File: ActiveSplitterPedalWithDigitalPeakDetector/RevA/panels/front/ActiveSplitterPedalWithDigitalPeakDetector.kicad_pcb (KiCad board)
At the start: 2 copper layers, 112.5 x 86.4 mm, 5 parts

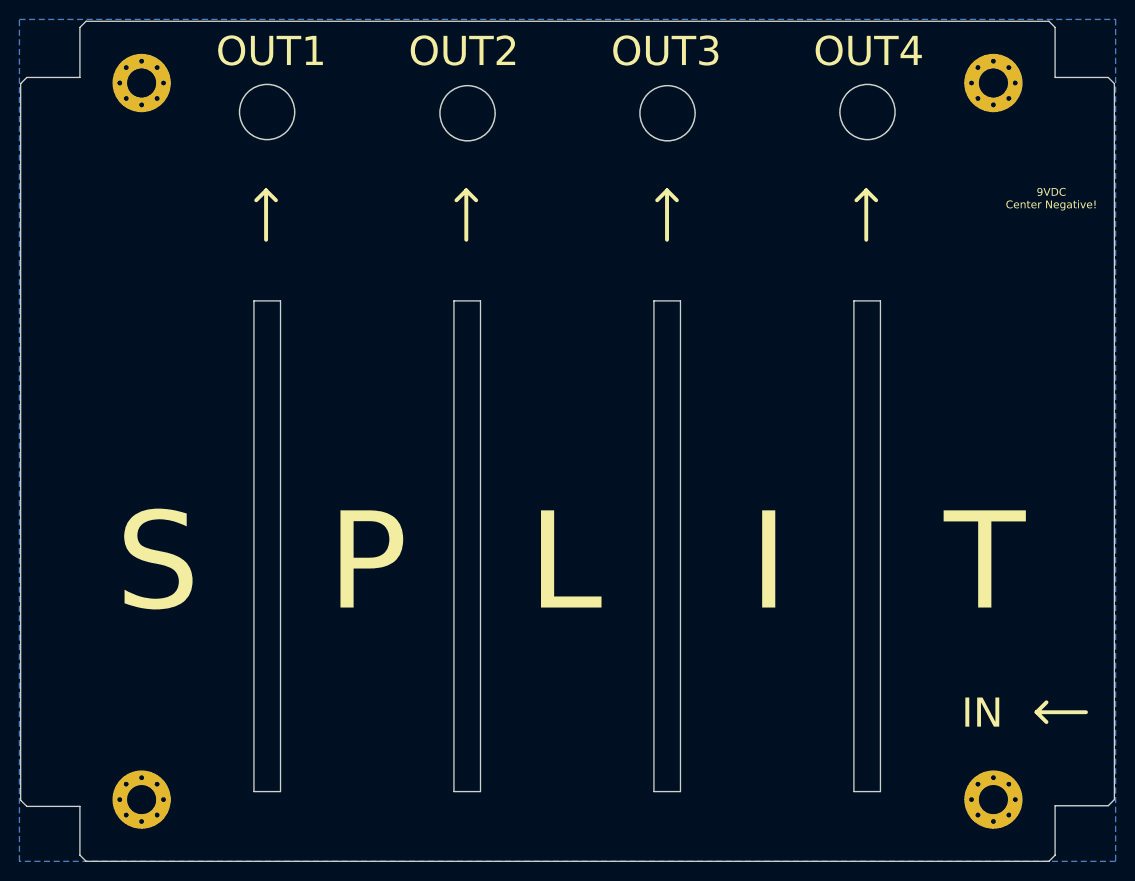
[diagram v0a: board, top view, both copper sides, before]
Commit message: updated front/back panel layout and gerbers
- Changed mount holes to non-via
- Changed BCu plane to FCu plane (same side as FCu silkscreen)
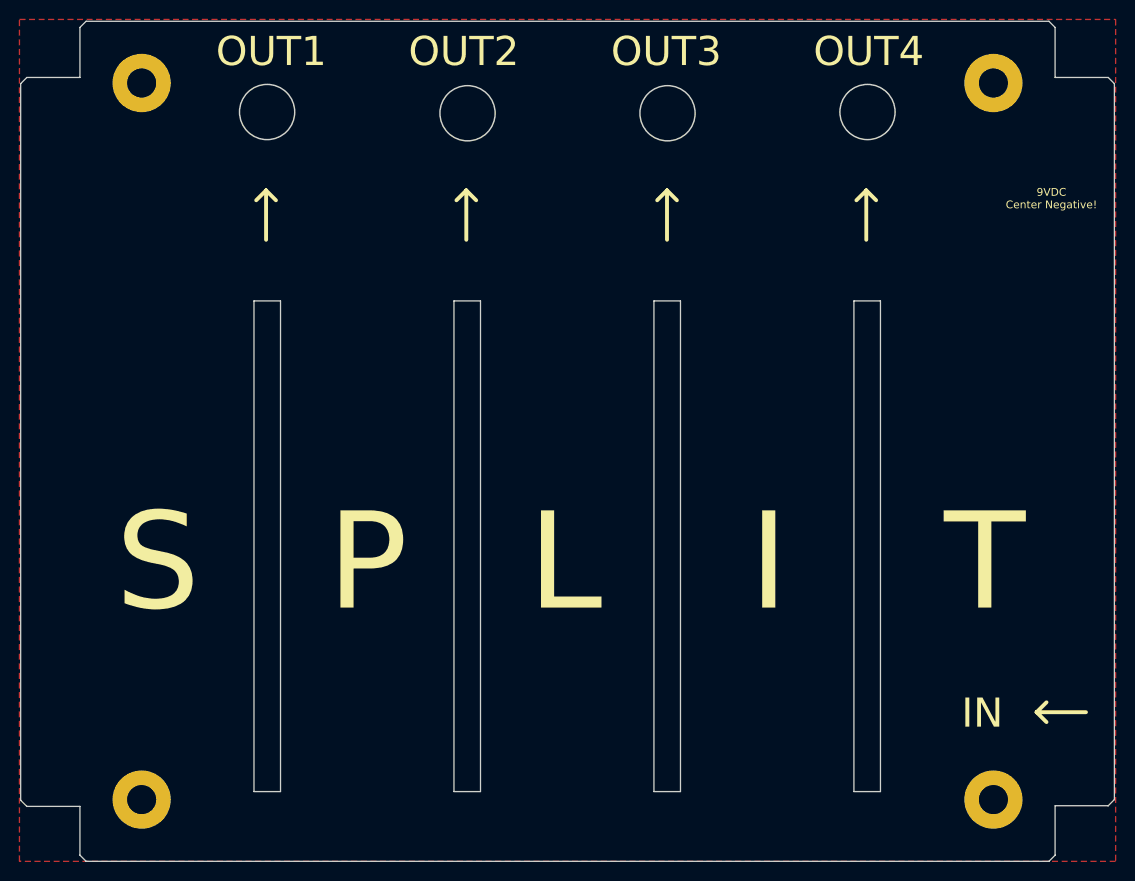
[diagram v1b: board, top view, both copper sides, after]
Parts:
- removed the REF** at (92.3, 124.7)
- removed the REF** at (180.0, 124.7)
- removed the REF** at (180.0, 51.0)
- added REF**: MountingHole_3mm_Pad, MountingHole:MountingHole_3mm_Pad, F.Cu at (180.0, 51.0)
- added REF**: MountingHole_3mm_Pad, MountingHole:MountingHole_3mm_Pad, F.Cu at (180.0, 124.7)
- added REF**: MountingHole_3mm_Pad, MountingHole:MountingHole_3mm_Pad, F.Cu at (92.3, 124.7)
- REF**: value MountingHole_3mm_Pad_Via -> MountingHole_3mm_Pad; footprint MountingHole:MountingHole_3mm_Pad_Via -> MountingHole:MountingHole_3mm_Pad
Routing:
- added copper zone on F.Cu, net (none)
- removed copper zone on B.Cu, net (none)
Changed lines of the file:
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@@
     (diff_pair_gap 0.127)
   )
-  (module MountingHole:MountingHole_3mm_Pad_Via locked (layer F.Cu)
+  (module MountingHole:MountingHole_3mm_Pad locked (layer F.Cu)
+    (at 179.959 50.9905)
+    (descr "Mounting Hole 3mm")
+    (tags "mounting hole 3mm")
+    (attr virtual)
+    (fp_text reference REF** (at 0 -4) (layer F.SilkS) hide
+      (effects (font (size 1 1) (thickness 0.15)))
+    )
+    (fp_text value MountingHole_3mm_Pad (at 0 4) (layer F.Fab)
+      (effects (font (size 1 1) (thickness 0.15)))
+    )
+    (fp_circle (center 0 0) (end 3.25 0) (layer F.CrtYd) (width 0.05))
+    (fp_circle (center 0 0) (end 3 0) (layer Cmts.User) (width 0.15))
+    (fp_text user %R (at 0.3 0) (layer F.Fab)
+      (effects (font (size 1 1) (thickness 0.15)))
+    )
+    (pad 1 thru_hole circle (at 0 0) (size 6 6) (drill 3) (layers *.Cu *.Mask))
+  )
+  (module MountingHole:MountingHole_3mm_Pad locked (layer F.Cu)
+    (at 179.959 124.714)
+    (descr "Mounting Hole 3mm")
+    (tags "mounting hole 3mm")
+    (attr virtual)
+    (fp_text reference REF** (at 0 -4) (layer F.SilkS) hide
+      (effects (font (size 1 1) (thickness 0.15)))
+    )
+    (fp_text value MountingHole_3mm_Pad (at 0 4) (layer F.Fab)
+      (effects (font (size 1 1) (thickness 0.15)))
+    )
+    (fp_circle (center 0 0) (end 3.25 0) (layer F.CrtYd) (width 0.05))
+    (fp_circle (center 0 0) (end 3 0) (layer Cmts.User) (width 0.15))
+    (fp_text user %R (at 0.3 0) (layer F.Fab)
+      (effects (font (size 1 1) (thickness 0.15)))
+    )
+    (pad 1 thru_hole circle (at 0 0) (size 6 6) (drill 3) (layers *.Cu *.Mask))
+  )
+  (module MountingHole:MountingHole_3mm_Pad locked (layer F.Cu)
     (at 92.329 124.714)
     (descr "Mounting Hole 3mm")
@@
       (effects (font (size 1 1) (thickness 0.15)))
     )
-    (fp_text value MountingHole_3mm_Pad_Via (at 0 4) (layer F.Fab)
-      (effects (font (size 1 1) (thickness 0.15)))
-    )
-    (fp_circle (center 0 0) (end 3.25 0) (layer F.CrtYd) (width 0.05))
-    (fp_circle (center 0 0) (end 3 0) (layer Cmts.User) (width 0.15))
-    (fp_text user %R (at 0.3 0) (layer F.Fab)
-      (effects (font (size 1 1) (thickness 0.15)))
-    )
-    (pad 1 thru_hole circle (at 0 0) (size 6 6) (drill 3) (layers *.Cu *.Mask))
-    (pad 1 thru_hole circle (at 2.25 0) (size 0.8 0.8) (drill 0.5) (layers *.Cu *.Mask))
-    (pad 1 thru_hole circle (at 1.59099 1.59099) (size 0.8 0.8) (drill 0.5) (layers *.Cu *.Mask))
-    (pad 1 thru_hole circle (at 0 2.25) (size 0.8 0.8) (drill 0.5) (layers *.Cu *.Mask))
-    (pad 1 thru_hole circle (at -1.59099 1.59099) (size 0.8 0.8) (drill 0.5) (layers *.Cu *.Mask))
-    (pad 1 thru_hole circle (at -2.25 0) (size 0.8 0.8) (drill 0.5) (layers *.Cu *.Mask))
-    (pad 1 thru_hole circle (at -1.59099 -1.59099) (size 0.8 0.8) (drill 0.5) (layers *.Cu *.Mask))
-    (pad 1 thru_hole circle (at 0 -2.25) (size 0.8 0.8) (drill 0.5) (layers *.Cu *.Mask))
-    (pad 1 thru_hole circle (at 1.59099 -1.59099) (size 0.8 0.8) (drill 0.5) (layers *.Cu *.Mask))
-  )
-  (module MountingHole:MountingHole_3mm_Pad_Via locked (layer F.Cu)
-    (at 179.959 124.714)
-    (descr "Mounting Hole 3mm")
-    (tags "mounting hole 3mm")
-    (attr virtual)
-    (fp_text reference REF** (at 0 -4) (layer F.SilkS) hide
-      (effects (font (size 1 1) (thickness 0.15)))
-    )
-    (fp_text value MountingHole_3mm_Pad_Via (at 0 4) (layer F.Fab)
-      (effects (font (size 1 1) (thickness 0.15)))
-    )
-    (fp_circle (center 0 0) (end 3.25 0) (layer F.CrtYd) (width 0.05))
-    (fp_circle (center 0 0) (end 3 0) (layer Cmts.User) (width 0.15))
-    (fp_text user %R (at 0.3 0) (layer F.Fab)
-      (effects (font (size 1 1) (thickness 0.15)))
-    )
-    (pad 1 thru_hole circle (at 0 0) (size 6 6) (drill 3) (layers *.Cu *.Mask))
-    (pad 1 thru_hole circle (at 2.25 0) (size 0.8 0.8) (drill 0.5) (layers *.Cu *.Mask))
-    (pad 1 thru_hole circle (at 1.59099 1.59099) (size 0.8 0.8) (drill 0.5) (layers *.Cu *.Mask))
-    (pad 1 thru_hole circle (at 0 2.25) (size 0.8 0.8) (drill 0.5) (layers *.Cu *.Mask))
-    (pad 1 thru_hole circle (at -1.59099 1.59099) (size 0.8 0.8) (drill 0.5) (layers *.Cu *.Mask))
-    (pad 1 thru_hole circle (at -2.25 0) (size 0.8 0.8) (drill 0.5) (layers *.Cu *.Mask))
-    (pad 1 thru_hole circle (at -1.59099 -1.59099) (size 0.8 0.8) (drill 0.5) (layers *.Cu *.Mask))
-    (pad 1 thru_hole circle (at 0 -2.25) (size 0.8 0.8) (drill 0.5) (layers *.Cu *.Mask))
-    (pad 1 thru_hole circle (at 1.59099 -1.59099) (size 0.8 0.8) (drill 0.5) (layers *.Cu *.Mask))
-  )
-  (module MountingHole:MountingHole_3mm_Pad_Via locked (layer F.Cu)
-    (at 179.959 50.9905)
-    (descr "Mounting Hole 3mm")
-    (tags "mounting hole 3mm")
-    (attr virtual)
-    (fp_text reference REF** (at 0 -4) (layer F.SilkS) hide
-      (effects (font (size 1 1) (thickness 0.15)))
-    )
-    (fp_text value MountingHole_3mm_Pad_Via (at 0 4) (layer F.Fab)
-      (effects (font (size 1 1) (thickness 0.15)))
-    )
-    (fp_circle (center 0 0) (end 3.25 0) (layer F.CrtYd) (width 0.05))
-    (fp_circle (center 0 0) (end 3 0) (layer Cmts.User) (width 0.15))
-    (fp_text user %R (at 0.3 0) (layer F.Fab)
-      (effects (font (size 1 1) (thickness 0.15)))
-    )
-    (pad 1 thru_hole circle (at 0 0) (size 6 6) (drill 3) (layers *.Cu *.Mask))
-    (pad 1 thru_hole circle (at 2.25 0) (size 0.8 0.8) (drill 0.5) (layers *.Cu *.Mask))
-    (pad 1 thru_hole circle (at 1.59099 1.59099) (size 0.8 0.8) (drill 0.5) (layers *.Cu *.Mask))
-    (pad 1 thru_hole circle (at 0 2.25) (size 0.8 0.8) (drill 0.5) (layers *.Cu *.Mask))
-    (pad 1 thru_hole circle (at -1.59099 1.59099) (size 0.8 0.8) (drill 0.5) (layers *.Cu *.Mask))
-    (pad 1 thru_hole circle (at -2.25 0) (size 0.8 0.8) (drill 0.5) (layers *.Cu *.Mask))
-    (pad 1 thru_hole circle (at -1.59099 -1.59099) (size 0.8 0.8) (drill 0.5) (layers *.Cu *.Mask))
-    (pad 1 thru_hole circle (at 0 -2.25) (size 0.8 0.8) (drill 0.5) (layers *.Cu *.Mask))
-    (pad 1 thru_hole circle (at 1.59099 -1.59099) (size 0.8 0.8) (drill 0.5) (layers *.Cu *.Mask))
-  )
-  (module MountingHole:MountingHole_3mm_Pad_Via locked (layer F.Cu)
+    (fp_text value MountingHole_3mm_Pad (at 0 4) (layer F.Fab)
+      (effects (font (size 1 1) (thickness 0.15)))
+    )
+    (fp_circle (center 0 0) (end 3.25 0) (layer F.CrtYd) (width 0.05))
+    (fp_circle (center 0 0) (end 3 0) (layer Cmts.User) (width 0.15))
+    (fp_text user %R (at 0.3 0) (layer F.Fab)
+      (effects (font (size 1 1) (thickness 0.15)))
+    )
+    (pad 1 thru_hole circle (at 0 0) (size 6 6) (drill 3) (layers *.Cu *.Mask))
+  )
+  (module MountingHole:MountingHole_3mm_Pad locked (layer F.Cu)
     (at 92.329 50.9905)
     (descr "Mounting Hole 3mm")
@@
       (effects (font (size 1 1) (thickness 0.15)))
     )
-    (fp_text value MountingHole_3mm_Pad_Via (at 0 4) (layer F.Fab)
-      (effects (font (size 1 1) (thickness 0.15)))
-    )
-    (fp_circle (center 0 0) (end 3.25 0) (layer F.CrtYd) (width 0.05))
-    (fp_circle (center 0 0) (end 3 0) (layer Cmts.User) (width 0.15))
-    (fp_text user %R (at 0.3 0) (layer F.Fab)
-      (effects (font (size 1 1) (thickness 0.15)))
-    )
-    (pad 1 thru_hole circle (at 1.59099 -1.59099) (size 0.8 0.8) (drill 0.5) (layers *.Cu *.Mask))
-    (pad 1 thru_hole circle (at 0 -2.25) (size 0.8 0.8) (drill 0.5) (layers *.Cu *.Mask))
-    (pad 1 thru_hole circle (at -1.59099 -1.59099) (size 0.8 0.8) (drill 0.5) (layers *.Cu *.Mask))
-    (pad 1 thru_hole circle (at -2.25 0) (size 0.8 0.8) (drill 0.5) (layers *.Cu *.Mask))
-    (pad 1 thru_hole circle (at -1.59099 1.59099) (size 0.8 0.8) (drill 0.5) (layers *.Cu *.Mask))
-    (pad 1 thru_hole circle (at 0 2.25) (size 0.8 0.8) (drill 0.5) (layers *.Cu *.Mask))
-    (pad 1 thru_hole circle (at 1.59099 1.59099) (size 0.8 0.8) (drill 0.5) (layers *.Cu *.Mask))
-    (pad 1 thru_hole circle (at 2.25 0) (size 0.8 0.8) (drill 0.5) (layers *.Cu *.Mask))
+    (fp_text value MountingHole_3mm_Pad (at 0 4) (layer F.Fab)
+      (effects (font (size 1 1) (thickness 0.15)))
+    )
+    (fp_circle (center 0 0) (end 3.25 0) (layer F.CrtYd) (width 0.05))
+    (fp_circle (center 0 0) (end 3 0) (layer Cmts.User) (width 0.15))
+    (fp_text user %R (at 0.3 0) (layer F.Fab)
+      (effects (font (size 1 1) (thickness 0.15)))
+    )
     (pad 1 thru_hole circle (at 0 0) (size 6 6) (drill 3) (layers *.Cu *.Mask))
   )
@@
   (gr_line (start 86.614 131.064) (end 85.979 130.429) (layer Edge.Cuts) (width 0.05))
   (gr_line (start 185.674 131.064) (end 86.614 131.064) (layer Edge.Cuts) (width 0.05))
-  (zone (net 0) (net_name "") (layer B.Cu) (hatch edge 0.508)
+  (zone (net 0) (net_name "") (layer F.Cu) (hatch edge 0.508)
     (connect_pads yes (clearance 0.508))
     (min_thickness 0.254)
